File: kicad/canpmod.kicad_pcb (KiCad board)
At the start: 2 copper layers, 27.9 x 30.5 mm, 12 parts, among them J1 Conn_01x02, J2 PMOD, U1 SN65HVD230

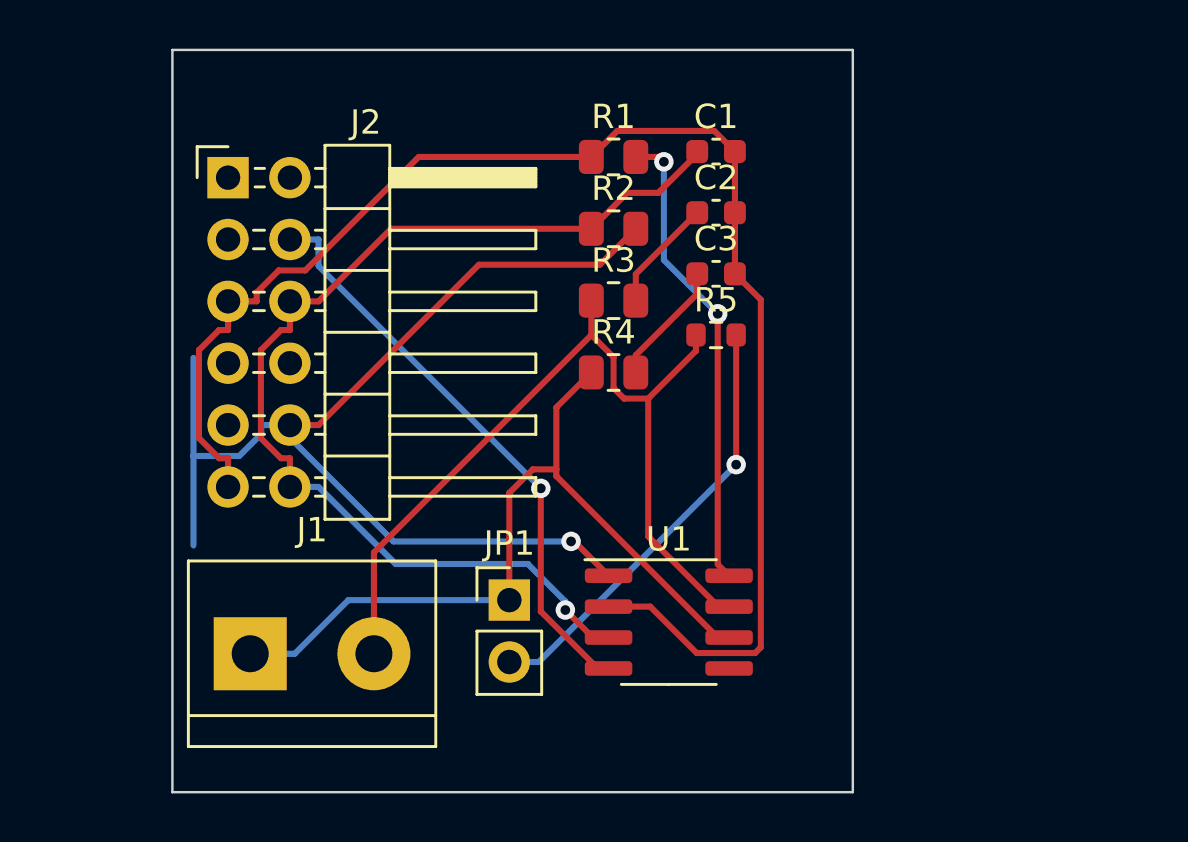
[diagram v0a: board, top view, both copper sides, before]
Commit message: Improve routing and add 3d image
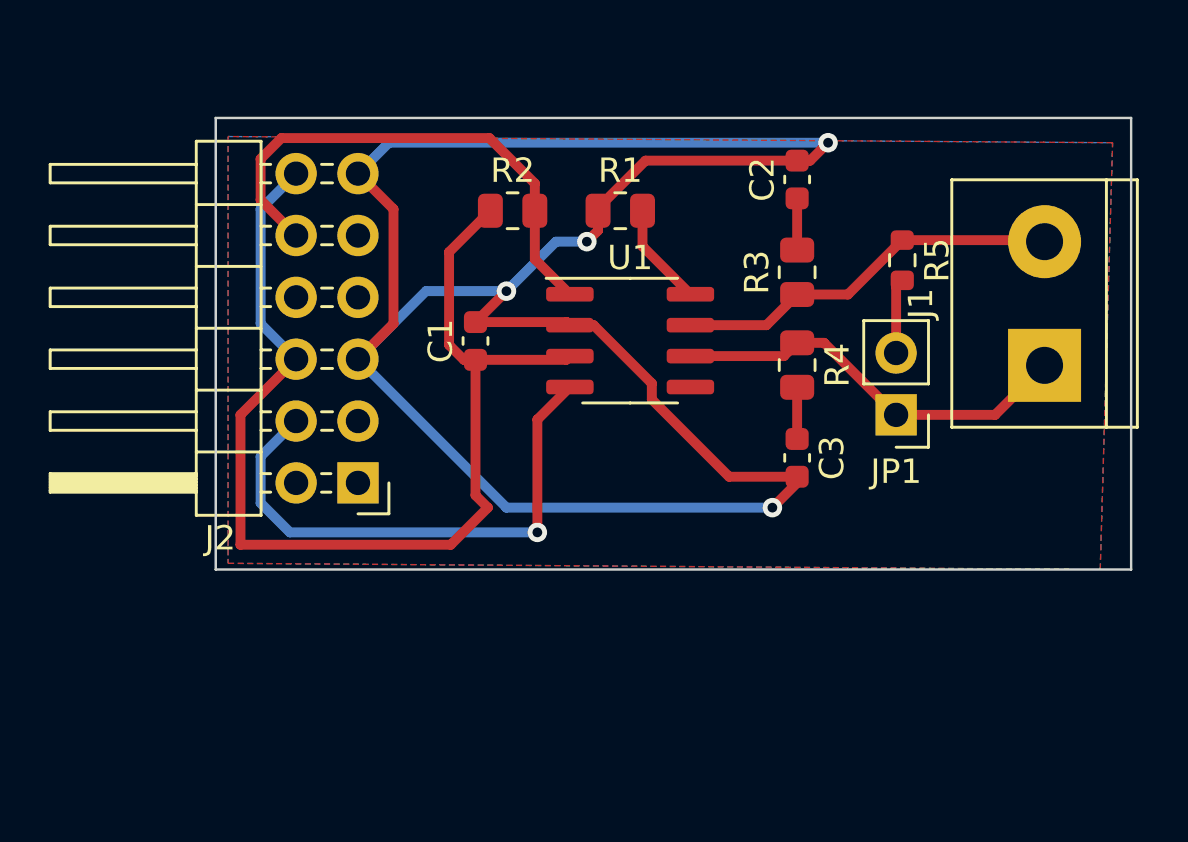
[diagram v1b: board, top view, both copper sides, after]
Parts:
- moved J1 34.7 mm to (183.1, 84.1), turned to 90 degrees
- moved JP1 17.6 mm to (177.0, 86.1), turned to 180 degrees
- moved J2 13.6 mm to (154.9, 88.9), turned to 180 degrees
- moved C1 12.6 mm to (159.8, 83.1), turned to 90 degrees
- moved U1 11.7 mm to (166.1, 83.1)
- moved C3 8.26 mm to (173.0, 87.9), turned to -90 degrees
- moved R5 8.24 mm to (177.3, 79.8), turned to -90 degrees
- moved R3 7.63 mm to (173.0, 80.3), turned to 90 degrees
- moved R4 7.55 mm to (173.0, 84.1), turned to -90 degrees
- moved R2 4.21 mm to (161.3, 77.7)
- moved C2 3.60 mm to (173.0, 76.4), turned to 90 degrees
- moved R1 2.23 mm to (165.7, 77.7)
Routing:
- net GND: track 61.3 -> 91.4 mm, vias 0 -> 4
- net CTX: track 46.1 -> 21.3 mm, vias 1 -> 0
- net CAN_H: track 36.0 -> 16.0 mm
- net CAN_L: track 33.0 -> 17.6 mm
- net Net-(U1-Rs): track 19.3 -> 4.24 mm, vias 2 -> 0
- net Net-(JP1-B): track 18.0 -> 3.09 mm, vias 1 -> 0
- net Net-(C3-Pad1): track 5.09 -> 2.12 mm
- net Net-(C2-Pad1): track 4.65 -> 2.12 mm
- net +3.3V: track 44.2 -> 46.0 mm, vias 1 -> 0
- net CRX: track 24.0 -> 22.4 mm
- added copper zone on B.Cu, net (none)
- added copper zone on F.Cu, net GND
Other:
- board size 27.9 x 30.5 mm -> 37.6 x 18.5 mm
